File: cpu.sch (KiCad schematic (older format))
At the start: 2 parts, among them J1 Conn_02x05_Odd_Even, U1 E73-2G4M04S-52832

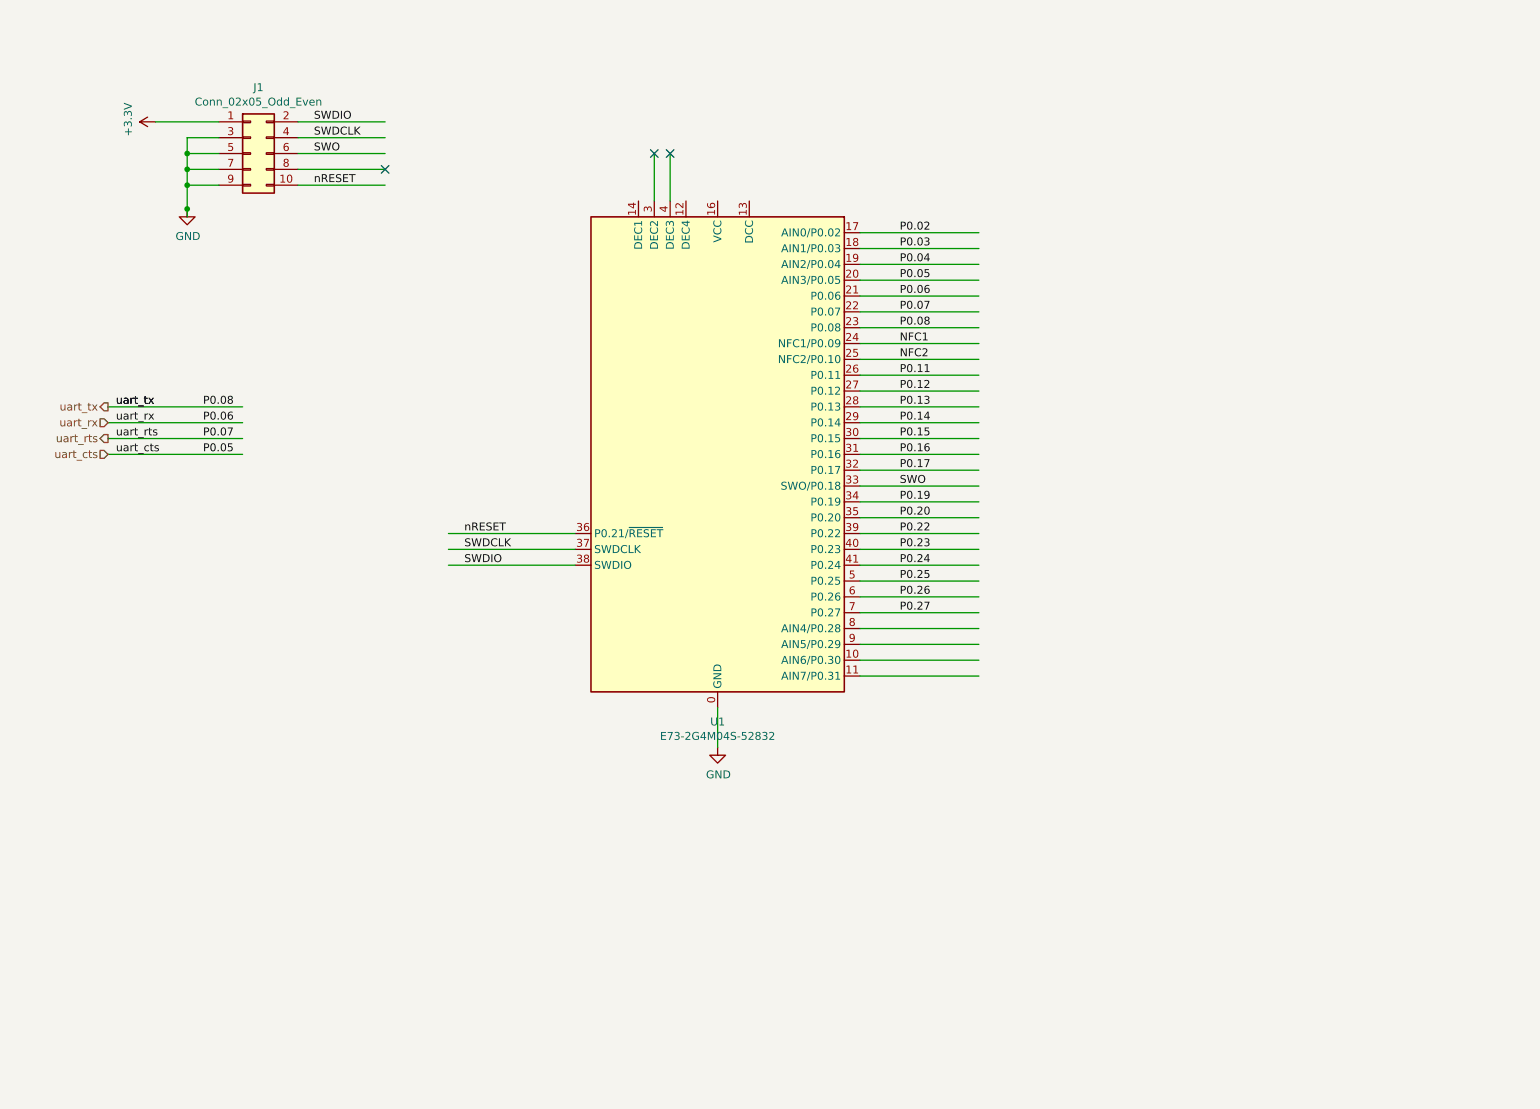
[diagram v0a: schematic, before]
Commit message: added TP4056 module
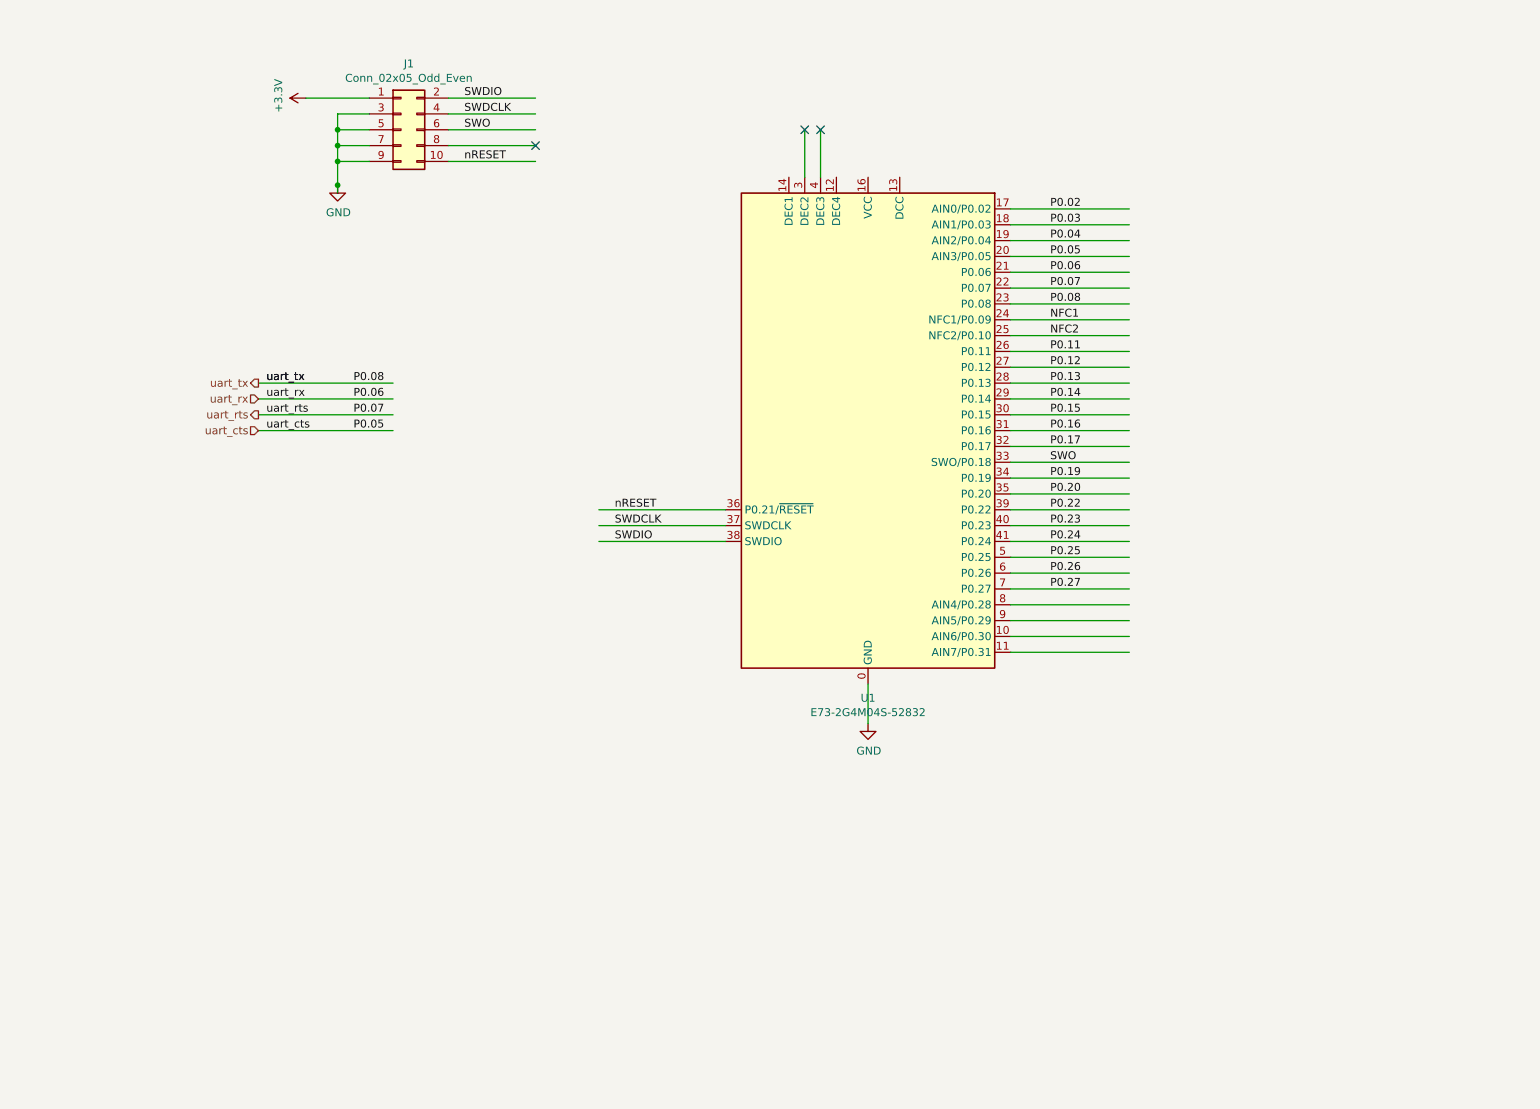
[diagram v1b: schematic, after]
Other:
- moved on the sheet: J1, U1

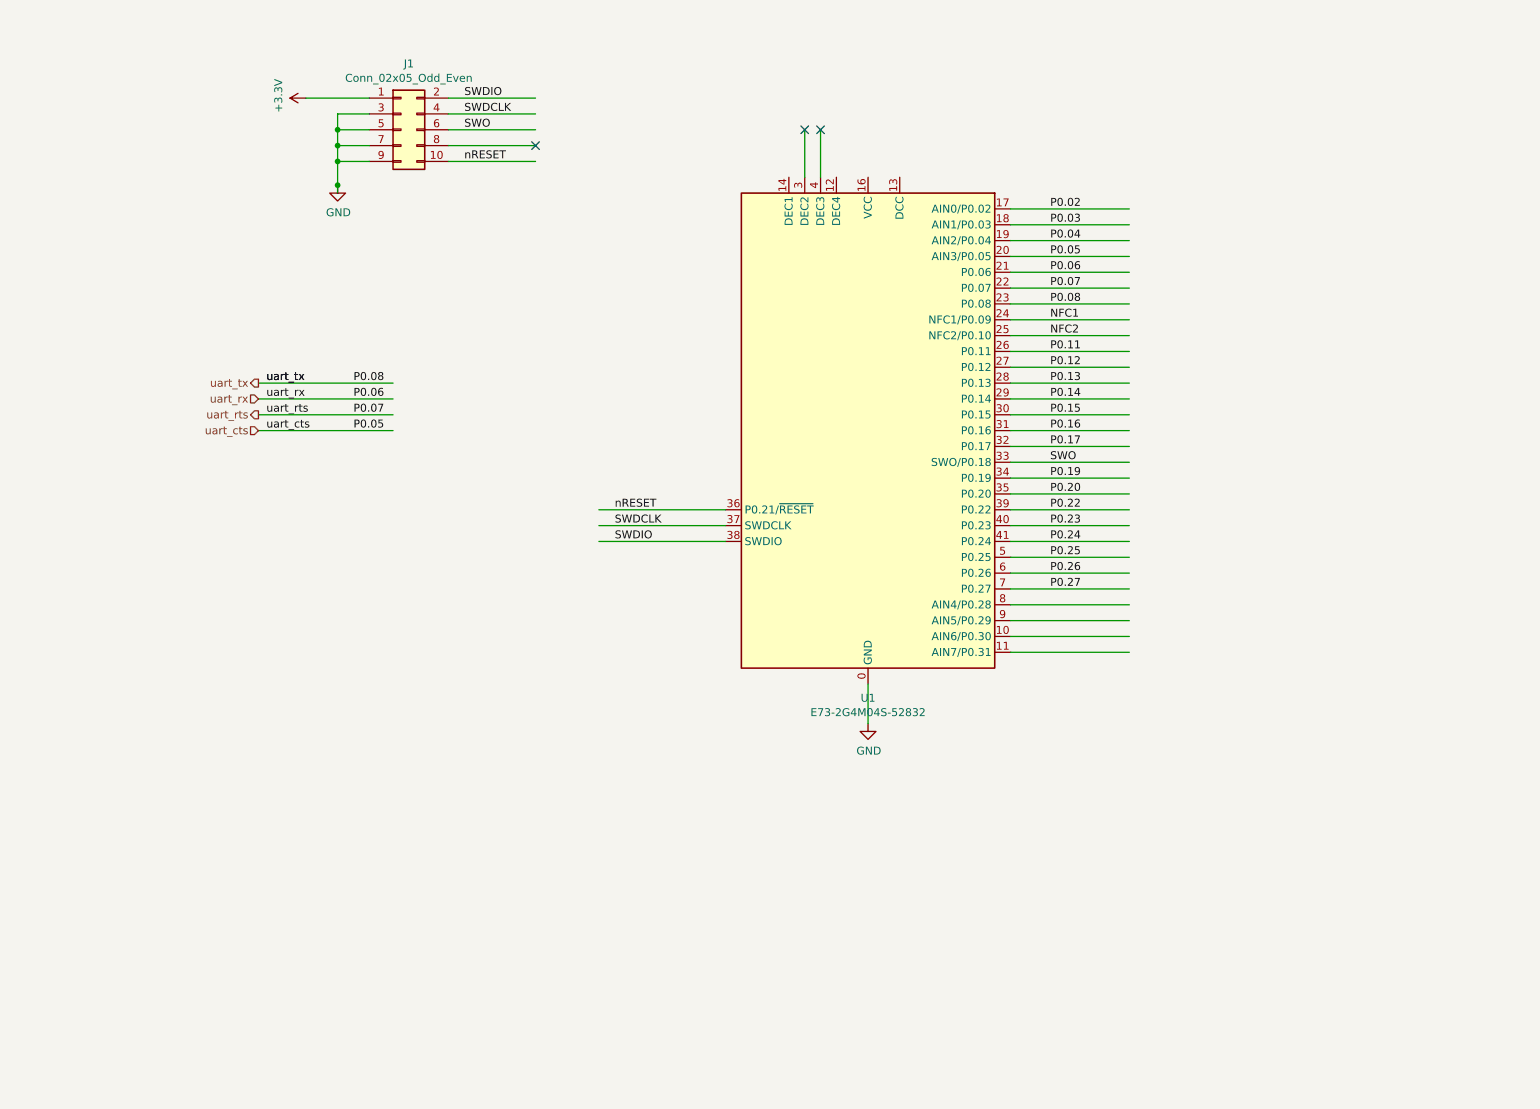
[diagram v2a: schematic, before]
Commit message: added more circuit parts + new step files
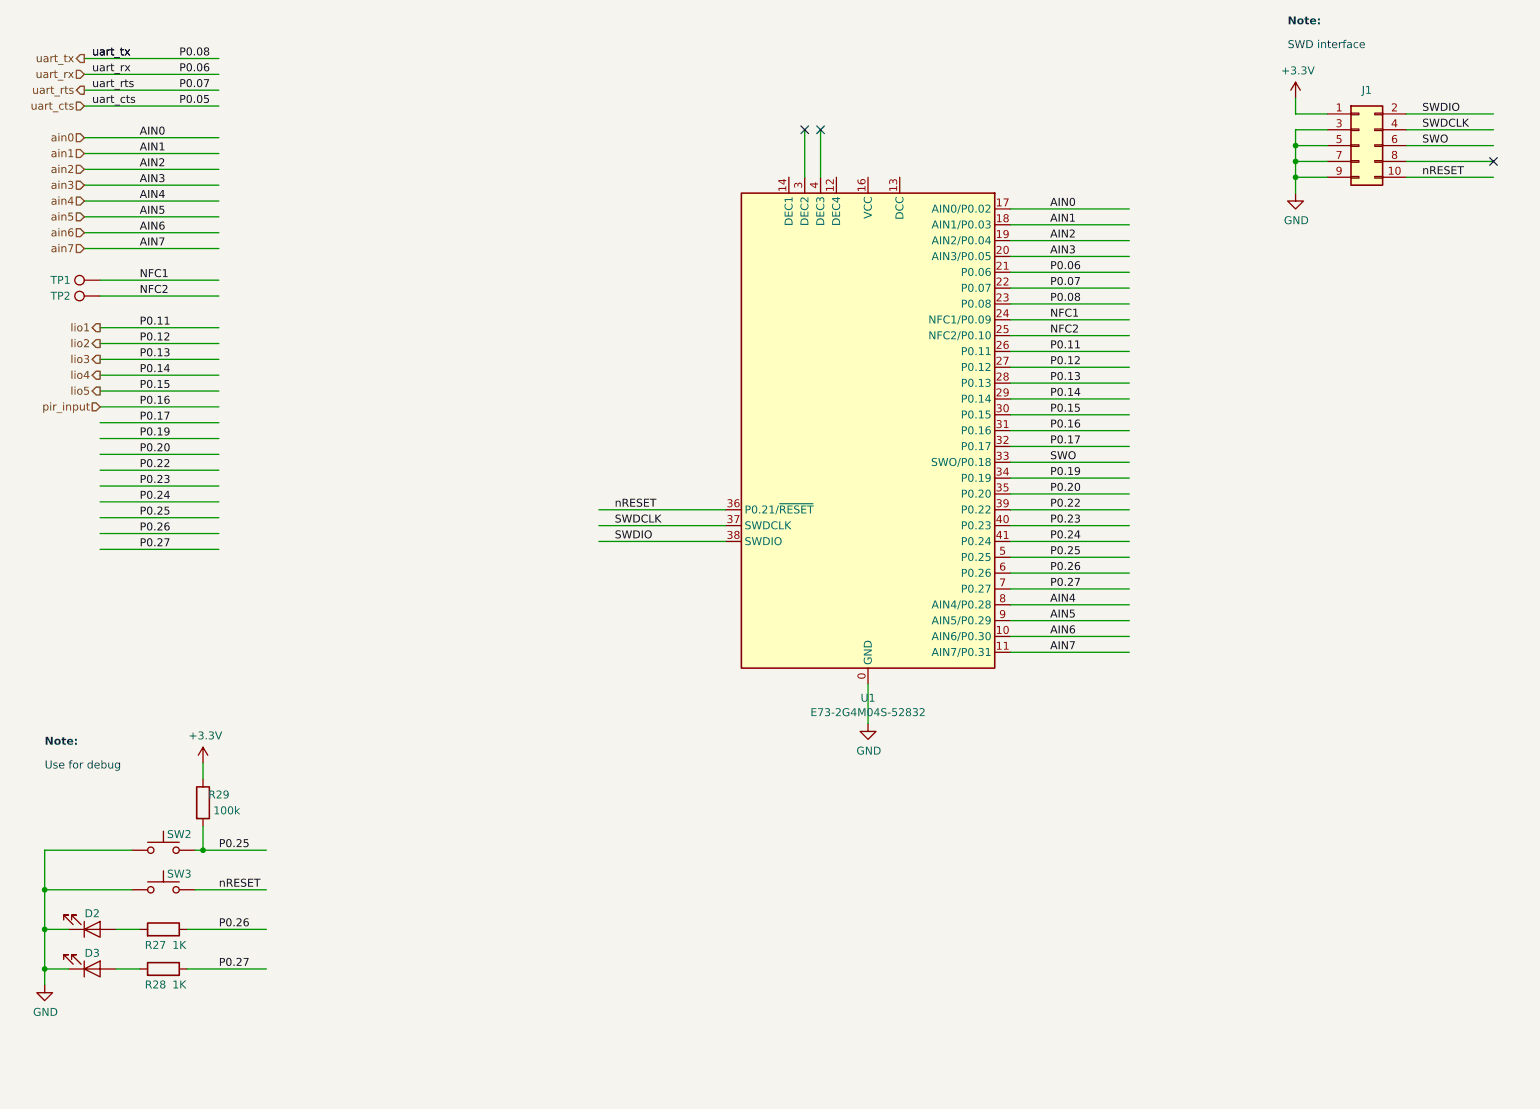
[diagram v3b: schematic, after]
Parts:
- added D2, D3: LED, LED_SMD:LED_0603_1608Metric_Pad1.05x0.95mm_HandSolder, symbol Device:LED
- added R27, R28: 1K, Resistor_SMD:R_0805_2012Metric_Pad1.15x1.40mm_HandSolder, symbol Device:R
- added R29: 100k, Resistor_SMD:R_0805_2012Metric_Pad1.15x1.40mm_HandSolder, symbol Device:R
- added SW2, SW3: SW_Push, Button_Switch_SMD:Panasonic_EVQPUL_EVQPUC, symbol Switch:SW_Push
- added TP1, TP2: TestPoint, TestPoint:TestPoint_Pad_D1.5mm, symbol Connector:TestPoint
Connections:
- net labels added: AIN0, AIN1, AIN2, AIN3, AIN4, AIN5, AIN6, AIN7, ain0, ain1, ain2, ain3, ain4, ain5, ain6, ain7, lio1, lio2, lio3, lio4, lio5, pir_input
- net labels removed: P0.02, P0.03, P0.04
- wire segments 54 -> 96
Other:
- note added: "Note:"
- note added: "SWD interface"
- note added: "Use for debug"
- moved on the sheet: J1

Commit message: started pcb routing
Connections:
- net labels removed: AIN3, ain3
- wire segments 96 -> 95
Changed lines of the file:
@@
 Text Label 7750 2250 0    50   ~ 0
 AIN2
-Text Label 7750 2350 0    50   ~ 0
-AIN3
 Text Label 7750 2450 0    50   ~ 0
 P0.06
@@
 Text Label 1700 1400 0    50   ~ 0
 uart_cts
+Text Label 2250 1400 0    50   ~ 0
+P0.07
 Text Label 2250 1300 0    50   ~ 0
-P0.07
-Text Label 2250 1400 0    50   ~ 0
 P0.05
+Text Label 2250 1200 0    50   ~ 0
+P0.08
 Text Label 2250 1100 0    50   ~ 0
-P0.08
-Text Label 2250 1200 0    50   ~ 0
 P0.06
 Wire Wire Line
@@
 Wire Wire Line
 	2500 1800 1650 1800
-Wire Wire Line
-	2500 1900 1650 1900
 Text Label 2000 1700 0    50   ~ 0
 AIN1
 Text Label 2000 1800 0    50   ~ 0
 AIN2
-Text Label 2000 1900 0    50   ~ 0
-AIN3
 Text Label 2000 1600 0    50   ~ 0
 AIN0
@@
 Text HLabel 1650 1800 0    50   Input ~ 0
 ain2
-Text HLabel 1650 1900 0    50   Input ~ 0
-ain3
 Text HLabel 1650 2000 0    50   Input ~ 0
 ain4
@@
 	0    -1   -1   0
 $EndComp
+Text Label 7750 2350 0    50   ~ 0
+P0.05
 $EndSCHEMATC
